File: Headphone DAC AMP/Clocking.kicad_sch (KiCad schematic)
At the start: 13 parts, among them Y1 Crystal_GND24, Y2 LMK6CE049152CDLFR, Y3 ASDLJ-E-45.1584MHz

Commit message: Swapped to 0603 caps in order to compact design
Planning on a 100x70mm board shape
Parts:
- C20, C21: footprint Capacitor_SMD:C_0805_2012Metric_Pad1.18x1.45mm_HandSolder -> Capacitor_SMD:C_0603_1608Metric_Pad1.08x0.95mm_HandSolder
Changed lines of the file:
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@@
 			)
 		)
-		(property "Footprint" "Capacitor_SMD:C_0805_2012Metric_Pad1.18x1.45mm_HandSolder"
+		(property "Footprint" "Capacitor_SMD:C_0603_1608Metric_Pad1.08x0.95mm_HandSolder"
 			(at 89.8652 125.73 0)
 			(effects
@@
 			)
 		)
-		(property "Footprint" "Capacitor_SMD:C_0805_2012Metric_Pad1.18x1.45mm_HandSolder"
+		(property "Footprint" "Capacitor_SMD:C_0603_1608Metric_Pad1.08x0.95mm_HandSolder"
 			(at 101.6 139.3952 0)
 			(effects

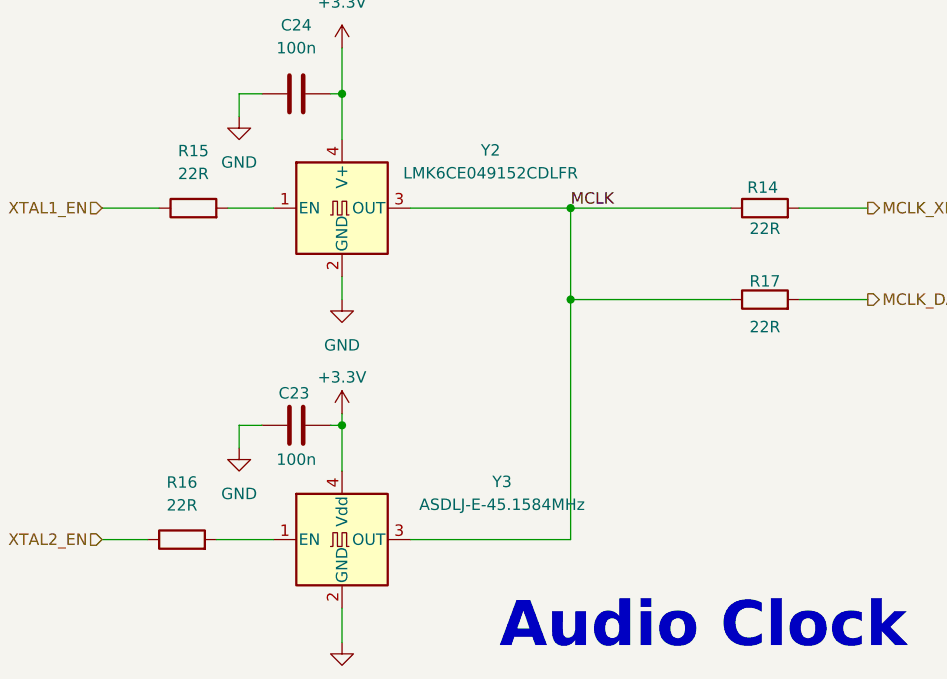
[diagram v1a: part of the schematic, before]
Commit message: Added I2C Pullups
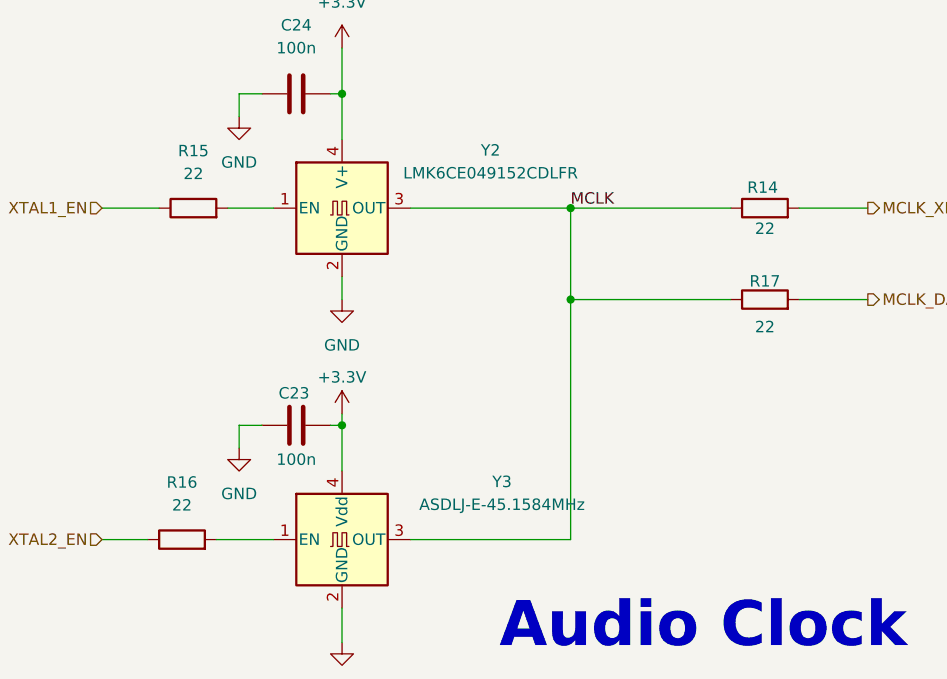
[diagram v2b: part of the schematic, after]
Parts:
- R14, R15, R16, R17: value 22R -> 22
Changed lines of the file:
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@@
 			)
 		)
-		(property "Value" "22R"
+		(property "Value" "22"
 			(at 80.01 81.28 90)
 			(effects
@@
 			)
 		)
-		(property "Value" "22R"
+		(property "Value" "22"
 			(at 144.78 61.468 90)
 			(effects
@@
 			)
 		)
-		(property "Value" "22R"
+		(property "Value" "22"
 			(at 81.28 44.45 90)
 			(effects
@@
 			)
 		)
-		(property "Value" "22R"
+		(property "Value" "22"
 			(at 144.78 50.546 90)
 			(effects

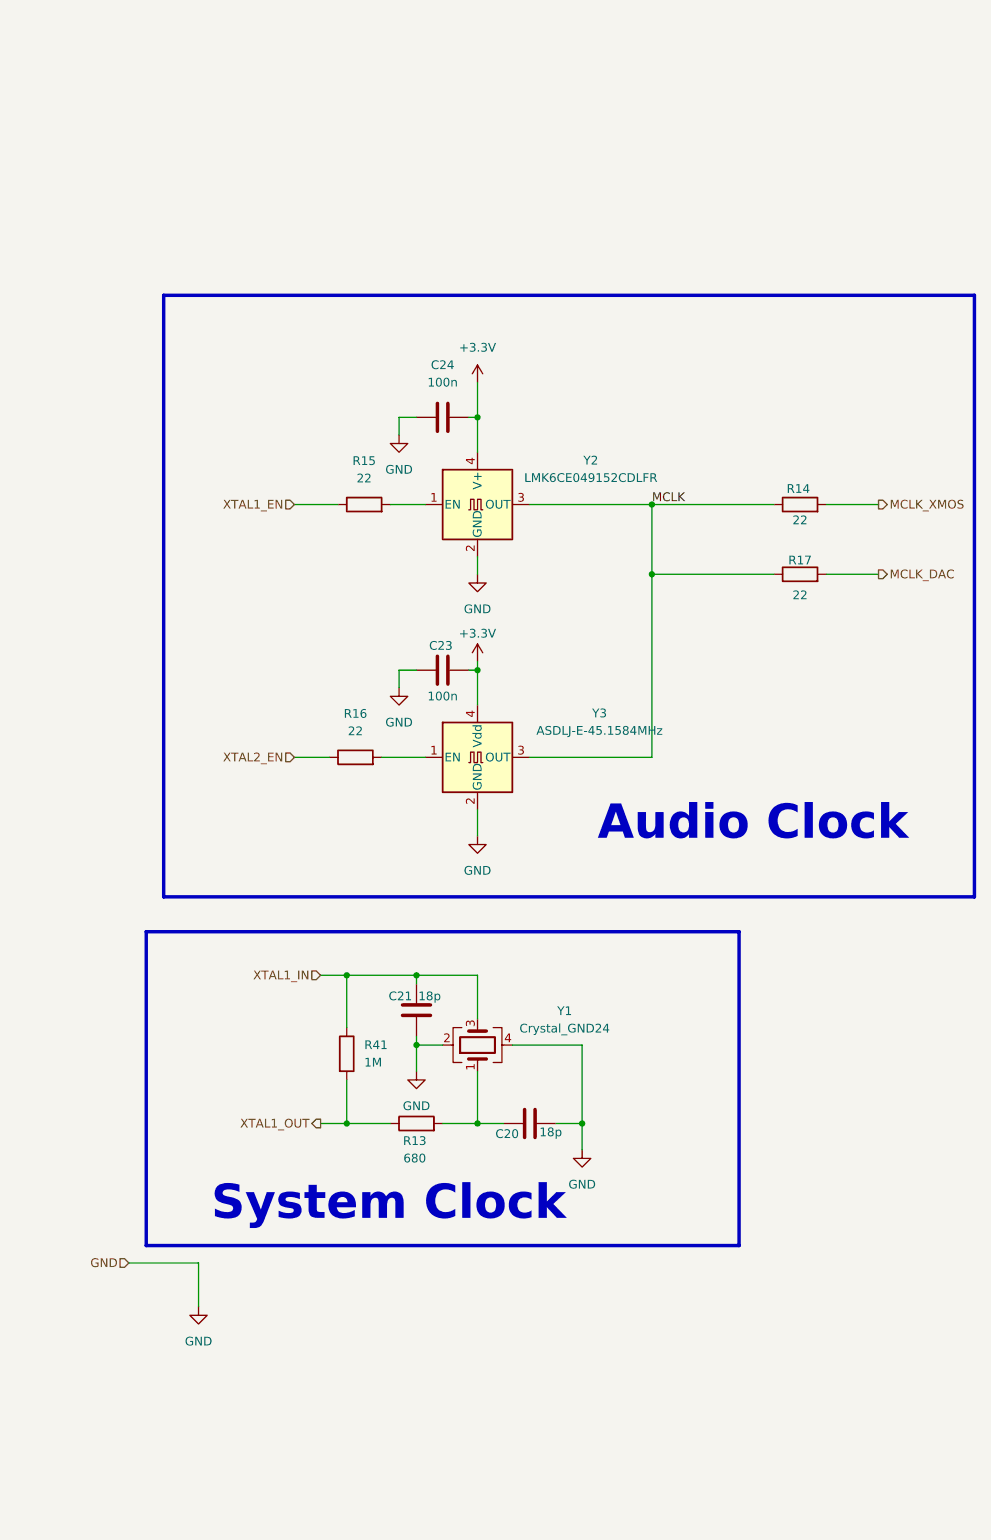
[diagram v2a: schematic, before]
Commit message: (Post Board Order) updated BOM with component links
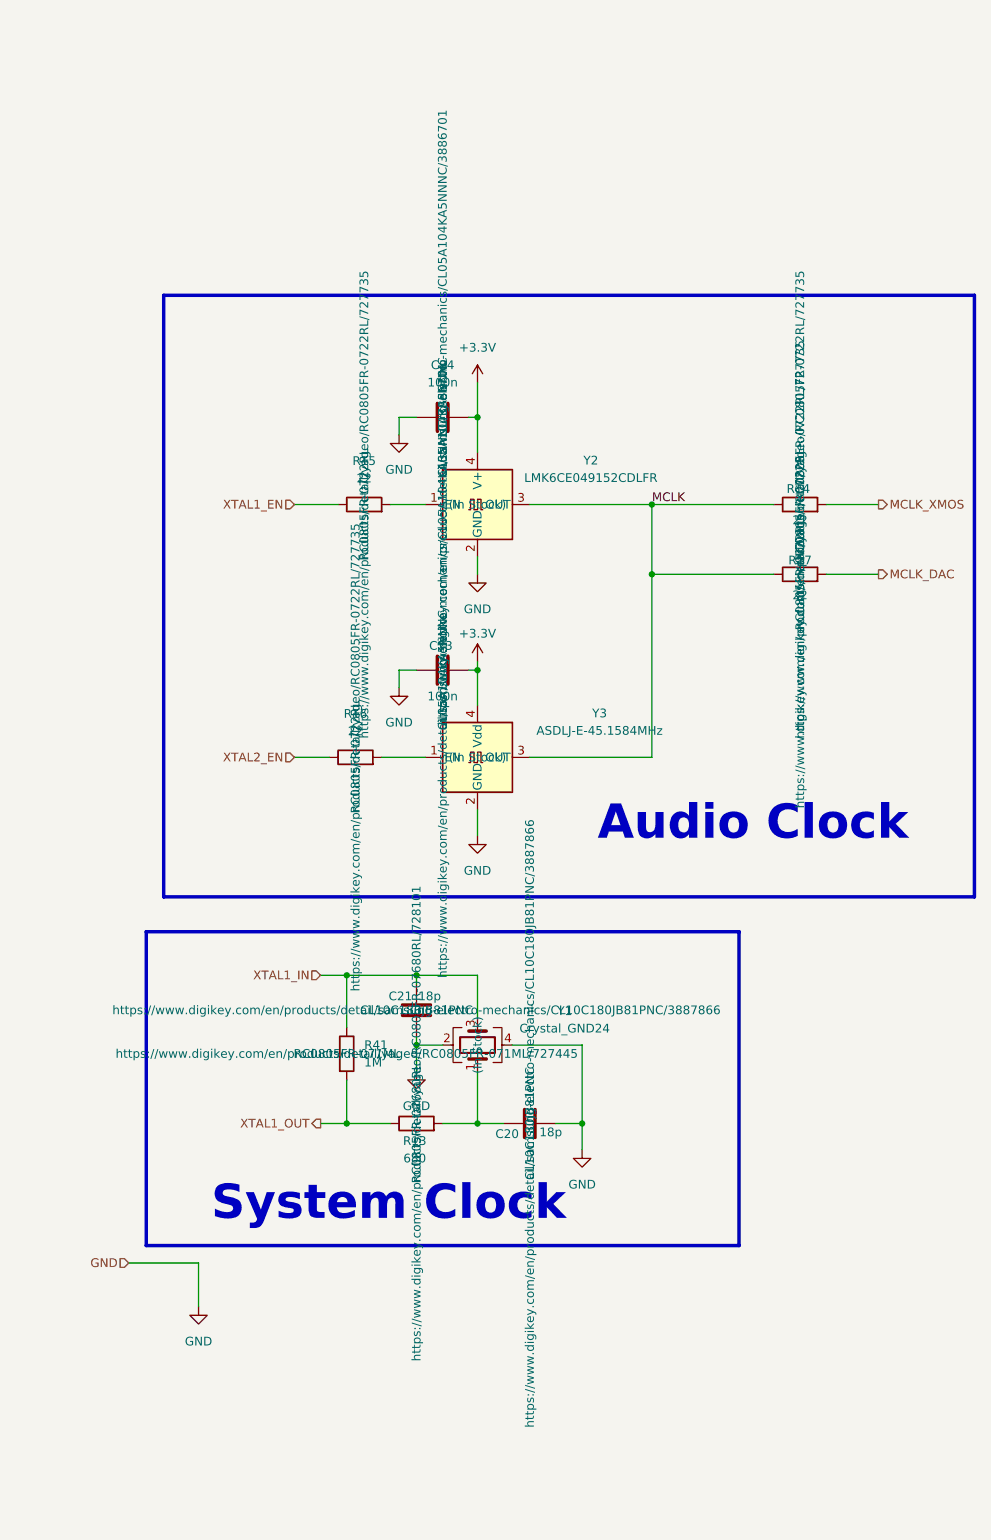
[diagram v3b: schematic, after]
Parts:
- C20, C21: CUI_PURCHASE_URL (none) -> https://www.digikey.com/en/products/detail/samsung-electro-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; Mouser Part Number (none) -> CL10C180JB81PNC
- C23, C24: CUI_PURCHASE_URL (none) -> https://www.digikey.com/en/products/detail/samsung-electro-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; Mouser Part Number (none) -> CL05A104KA5NNNC
- R13: CUI_PURCHASE_URL (none) -> https://www.digikey.com/en/products/detail/yageo/RC0805FR-0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; Mouser Part Number (none) -> RC0805FR-07680RL
- R14, R15, R16, R17: CUI_PURCHASE_URL (none) -> https://www.digikey.com/en/products/detail/yageo/RC0805FR-0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; Mouser Part Number (none) -> RC0805FR-0722RL
- R41: CUI_PURCHASE_URL (none) -> https://www.digikey.com/en/products/detail/yageo/RC0805FR-0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; Mouser Part Number (none) -> RC0805FR-071ML
- Y1, Y2, Y3: CUI_PURCHASE_URL (none) -> (In Stock)
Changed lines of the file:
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@@
+			)
+		)
+		(property "CUI_PURCHASE_URL" "https://www.digikey.com/en/products/detail/yageo/RC0805FR-0722RL/727735"
+			(at 80.01 85.09 0)
+			(effects
+				(font
+					(size 1.27 1.27)
+				)
+			)
+		)
+		(property "Mouser Part Number" "RC0805FR-0722RL"
+			(at 80.01 85.09 0)
+			(effects
+				(font
+					(size 1.27 1.27)
+				)
 			)
 		)
@@
 			)
 		)
+		(property "CUI_PURCHASE_URL" "https://www.digikey.com/en/products/detail/samsung-electro-mechanics/CL05A104KA5NNNC/3886701"
+			(at 92.71 35.56 0)
+			(effects
+				(font
+					(size 1.27 1.27)
+				)
+			)
+		)
+		(property "Mouser Part Number" "CL05A104KA5NNNC"
+			(at 92.71 35.56 0)
+			(effects
+				(font
+					(size 1.27 1.27)
+				)
+			)
+		)
 		(pin "1"
 		)
@@
 			)
 		)
+		(property "CUI_PURCHASE_URL" "https://www.digikey.com/en/products/detail/yageo/RC0805FR-0722RL/727735"
+			(at 144.78 58.42 0)
+			(effects
+				(font
+					(size 1.27 1.27)
+				)
+			)
+		)
+		(property "Mouser Part Number" "RC0805FR-0722RL"
+			(at 144.78 58.42 0)
+			(effects
+				(font
+					(size 1.27 1.27)
+				)
+			)
+		)
 		(pin "1"
 		)
@@
 			)
 		)
+		(property "CUI_PURCHASE_URL" "https://www.digikey.com/en/products/detail/yageo/RC0805FR-0722RL/727735"
+			(at 81.28 48.26 0)
+			(effects
+				(font
+					(size 1.27 1.27)
+				)
+			)
+		)
+		(property "Mouser Part Number" "RC0805FR-0722RL"
+			(at 81.28 48.26 0)
+			(effects
+				(font
+					(size 1.27 1.27)
+				)
+			)
+		)
 		(pin "1"
 		)
@@
 			)
 		)
+		(property "CUI_PURCHASE_URL" "(In Stock)"
+			(at 97.79 48.26 0)
+			(effects
+				(font
+					(size 1.27 1.27)
+				)
+			)
+		)
 		(pin "3"
 		)
@@
 			)
 		)
+		(property "CUI_PURCHASE_URL" "https://www.digikey.com/en/products/detail/samsung-electro-mechanics/CL05A104KA5NNNC/3886701"
+			(at 92.71 72.39 0)
+			(effects
+				(font
+					(size 1.27 1.27)
+				)
+			)
+		)
+		(property "Mouser Part Number" "CL05A104KA5NNNC"
+			(at 92.71 72.39 0)
+			(effects
+				(font
+					(size 1.27 1.27)
+				)
+			)
+		)
 		(pin "1"
 		)
@@
 				)
 				(hide yes)
+			)
+		)
+		(property "CUI_PURCHASE_URL" "https://www.digikey.com/en/products/detail/samsung-electro-mechanics/CL10C180JB81PNC/3887866"
+			(at 88.9 121.92 0)
+			(effects
+				(font
+					(size 1.27 1.27)
+				)
+			)
+		)
+		(property "Mouser Part Number" "CL10C180JB81PNC"
+			(at 88.9 121.92 0)
+			(effects
+				(font
+					(size 1.27 1.27)
+				)
 			)
 		)
@@
 			)
 		)
+		(property "CUI_PURCHASE_URL" "(In Stock)"
+			(at 97.79 127 0)
+			(effects
+				(font
+					(size 1.27 1.27)
+				)
+			)
+		)
 		(pin "1"
 		)
@@
 				)
 				(hide yes)
+			)
+		)
+		(property "CUI_PURCHASE_URL" "https://www.digikey.com/en/products/detail/samsung-electro-mechanics/CL10C180JB81PNC/3887866"
+			(at 105.41 138.43 0)
+			(effects
+				(font
+					(size 1.27 1.27)
+				)
+			)
+		)
+		(property "Mouser Part Number" "CL10C180JB81PNC"
+			(at 105.41 138.43 0)
+			(effects
+				(font
+					(size 1.27 1.27)
+				)
 			)
 		)
@@
 			)
 		)
+		(property "CUI_PURCHASE_URL" "https://www.digikey.com/en/products/detail/yageo/RC0805FR-07680RL/728101"
+			(at 88.9 138.43 0)
+			(effects
+				(font
+					(size 1.27 1.27)
+				)
+			)
+		)
+		(property "Mouser Part Number" "RC0805FR-07680RL"
+			(at 88.9 138.43 0)
+			(effects
+				(font
+					(size 1.27 1.27)
+				)
+			)
+		)
 		(pin "1"
 		)
@@
 				)
 				(hide yes)
+			)
+		)
+		(property "CUI_PURCHASE_URL" "https://www.digikey.com/en/products/detail/yageo/RC0805FR-0722RL/727735"
+			(at 144.78 48.26 0)
+			(effects
+				(font
+					(size 1.27 1.27)
+				)
+			)
+		)
+		(property "Mouser Part Number" "RC0805FR-0722RL"
+			(at 144.78 48.26 0)
+			(effects
+				(font
+					(size 1.27 1.27)
+				)
 			)
 		)
@@
 			)
 		)
+		(property "CUI_PURCHASE_URL" "(In Stock)"
+			(at 97.79 85.09 0)
+			(effects
+				(font
+					(size 1.27 1.27)
+				)
+			)
+		)
 		(pin "4"
 		)
@@
 			)
 		)
+		(property "CUI_PURCHASE_URL" "https://www.digikey.com/en/products/detail/yageo/RC0805FR-071ML/727445"
+			(at 78.74 128.27 0)
+			(effects
+				(font
+					(size 1.27 1.27)
+				)
+			)
+		)
+		(property "Mouser Part Number" "RC0805FR-071ML"
+			(at 78.74 128.27 0)
+			(effects
+				(font
+					(size 1.27 1.27)
+				)
+			)
+		)

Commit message: Update capacitor footprints
Changed several capacitor footprints in schematic files from 0402/hand-solder variants to standard 0603_1608Metric. Updated PCB with new net and additional property fields for components.
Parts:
- C20, C21: footprint Capacitor_SMD:C_0603_1608Metric_Pad1.08x0.95mm_HandSolder -> Capacitor_SMD:C_0603_1608Metric
- C23, C24: footprint Capacitor_SMD:C_0402_1005Metric_Pad0.74x0.62mm_HandSolder -> Capacitor_SMD:C_0603_1608Metric
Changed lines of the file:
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@@
 			)
 		)
-		(property "Footprint" "Capacitor_SMD:C_0402_1005Metric_Pad0.74x0.62mm_HandSolder"
+		(property "Footprint" "Capacitor_SMD:C_0603_1608Metric"
 			(at 88.9 36.5252 0)
 			(effects
@@
 			)
 		)
-		(property "Footprint" "Capacitor_SMD:C_0402_1005Metric_Pad0.74x0.62mm_HandSolder"
+		(property "Footprint" "Capacitor_SMD:C_0603_1608Metric"
 			(at 88.9 73.3552 0)
 			(effects
@@
 			)
 		)
-		(property "Footprint" "Capacitor_SMD:C_0603_1608Metric_Pad1.08x0.95mm_HandSolder"
+		(property "Footprint" "Capacitor_SMD:C_0603_1608Metric"
 			(at 89.8652 125.73 0)
 			(effects
@@
 			)
 		)
-		(property "Footprint" "Capacitor_SMD:C_0603_1608Metric_Pad1.08x0.95mm_HandSolder"
+		(property "Footprint" "Capacitor_SMD:C_0603_1608Metric"
 			(at 101.6 139.3952 0)
 			(effects
